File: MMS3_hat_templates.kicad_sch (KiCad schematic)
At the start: 10 parts

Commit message: Updated footprints
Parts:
- removed PN1: ~, PCM_JLCPCB:Part_Num_JLCPCB, symbol PCM_JLCPCB-Manufacturing:Part Number, PCM_JLCPCB, 0.8x0.15mm
- added C16, C18: 10uF, PCM_JLCPCB:C_0603, symbol PCM_JLCPCB-Capacitors:0603,10uF
- added U4: AMS1117, PCM_JLCPCB:SOT-223-3_L6.5-W3.4-P2.30-LS7.0-BR, symbol PCM_JLCPCB-Power:LDO, 3.3V, 1A
- H7, H8, H9: value ~ -> (none)
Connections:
- net GND: now also C16.2, C18.2, U4.1 (GND)
- new net +3V3: C18.1, U4.2 (VOUT), U4.4 (VOUT)
- new net +5V: C16.1, U4.3 (VIN)
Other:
- removed sheet Buck Regulator
- note added: "3V3 LDO"
- moved on the sheet: H1, H2, H3, H4, H5, H6, H7, H8, H9

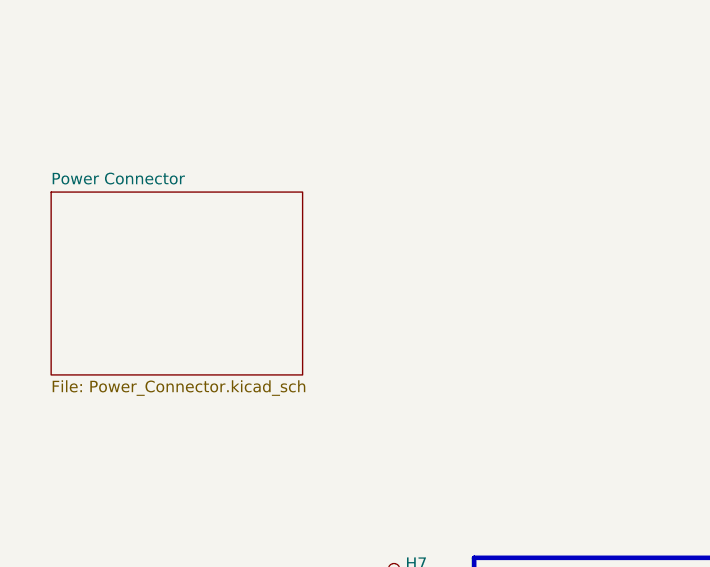
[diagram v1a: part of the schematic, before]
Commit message: changed vin connector to hierarchical labels
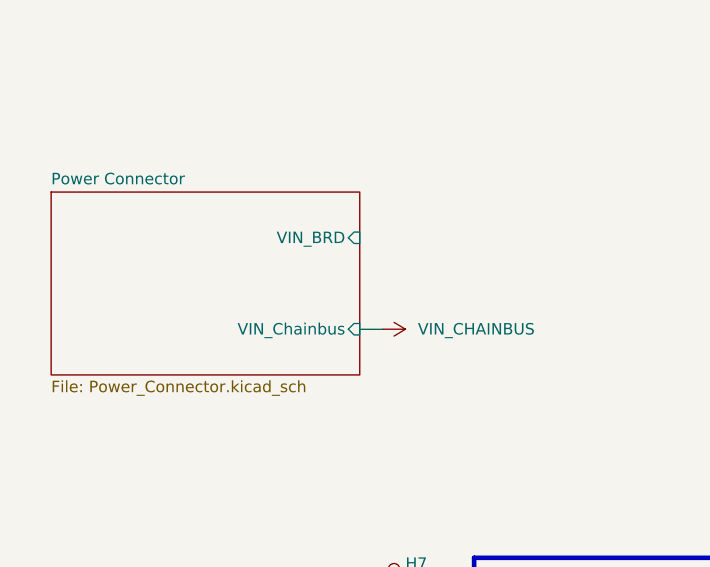
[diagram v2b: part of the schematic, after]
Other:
- sheet Power Connector ports: added VIN_BRD, VIN_Chainbus; removed none
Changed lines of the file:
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@@
 		)
 	)
+	(wire
+		(pts
+			(xy 52.07 140.97) (xy 54.61 140.97)
+		)
+		(stroke
+			(width 0)
+			(type default)
+		)
+	)
 	(bus
 		(pts
@@
 	)
 	(symbol
+		(lib_id "power:VCC")
+		(at 54.61 140.97 270)
+		(mirror x)
+		(unit 1)
+		(body_style 1)
+		(exclude_from_sim no)
+		(in_bom yes)
+		(on_board yes)
+		(in_pos_files yes)
+		(dnp no)
+		(property "Reference" "#PWR055"
+			(at 50.8 140.97 0)
+			(hide yes)
+			(show_name no)
+			(do_not_autoplace no)
+			(effects
+				(font
+					(size 1.27 1.27)
+				)
+			)
+		)
+		(property "Value" "VIN_CHAINBUS"
+			(at 65.024 140.97 90)
+			(show_name no)
+			(do_not_autoplace no)
+			(effects
+				(font
+					(size 1.27 1.27)
+				)
+			)
+		)
+		(property "Footprint" ""
+			(at 54.61 140.97 0)
+			(hide yes)
+			(show_name no)
+			(do_not_autoplace no)
+			(effects
+				(font
+					(size 1.27 1.27)
+				)
+			)
+		)
+		(property "Datasheet" ""
+			(at 54.61 140.97 0)
+			(hide yes)
+			(show_name no)
+			(do_not_autoplace no)
+			(effects
+				(font
+					(size 1.27 1.27)
+				)
+			)
+		)
+		(property "Description" "Power symbol creates a global label with name \"VCC\""
+			(at 54.61 140.97 0)
+			(hide yes)
+			(show_name no)
+			(do_not_autoplace no)
+			(effects
+				(font
+					(size 1.27 1.27)
+				)
+			)
+		)
+		(pin "1"
+		)
+		(instances
+			(project "MMS3_hat_templates"
+				(path "/6596548a-44e0-46d8-8624-fd71cf4a3e17"
+					(reference "#PWR055")
+					(unit 1)
+				)
+			)
+		)
+	)
+	(symbol
 		(lib_id "Mechanical:MountingHole")
 		(at 33.02 193.04 0)
@@
 	(sheet
 		(at 17.78 125.73)
-		(size 27.94 20.32)
+		(size 34.29 20.32)
 		(exclude_from_sim no)
 		(in_bom yes)
@@
 			)
 		)
+		(pin "VIN_BRD" input
+			(at 52.07 130.81 0)
+			(effects
+				(font
+					(size 1.27 1.27)
+				)
+				(justify right)
+			)
+		)
+		(pin "VIN_Chainbus" input
+			(at 52.07 140.97 0)
+			(effects
+				(font
+					(size 1.27 1.27)
+				)
+				(justify right)
+			)
+		)
